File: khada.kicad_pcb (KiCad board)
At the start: 2 copper layers, 154.2 x 111.4 mm, 56 parts, among them J1 MJ-4PP-9, SW1 SW_Push, SW10 SW_Push, SW11 SW_Push, SW12 SW_Push, SW13 SW_Push, SW14 SW_Push, SW15 SW_Push, SW16 SW_Push, SW17 SW_Push, SW18 SW_Push, SW19 SW_Push, SW2 SW_Push, SW20 SW_Push, SW21 SW_Push, SW22 SW_Push, SW3 SW_Push, SW4 SW_Push, SW5 SW_Push, SW6 SW_Push, SW7 SW_Push, SW8 SW_Push, SW9 SW_Push, U1 YAAJ_WeAct_BlackPill_Part_Lik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

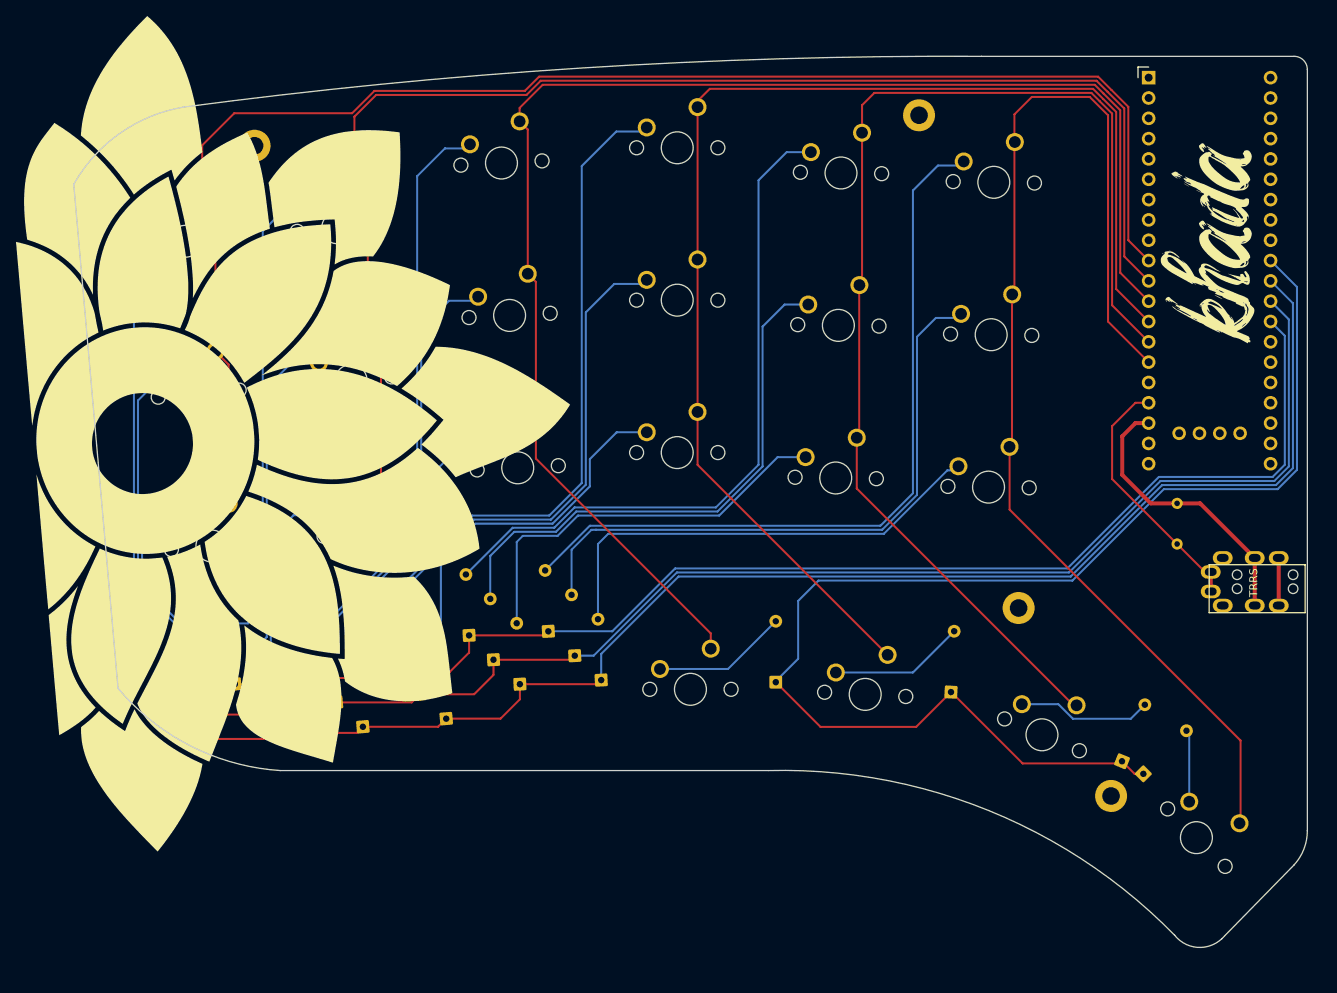
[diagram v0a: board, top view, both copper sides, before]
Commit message: cleaned up switch placement
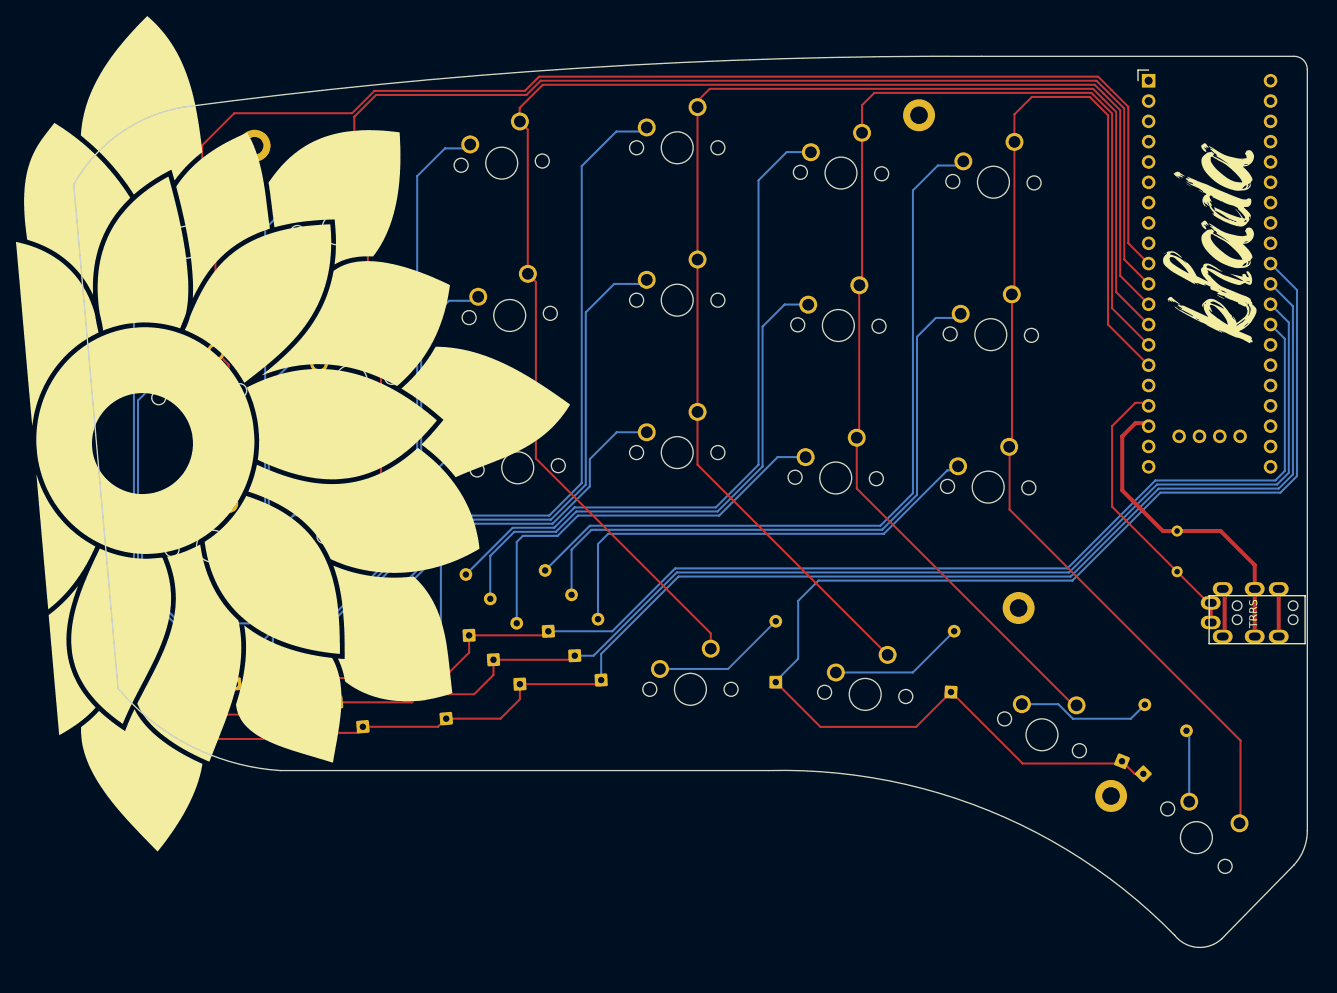
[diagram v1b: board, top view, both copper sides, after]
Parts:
- moved J1 3.87 mm to (204.7, 119.4)
- moved R1 3.45 mm to (188.7, 113.4)
- moved U1 0.38 mm to (185.2, 52.1)
- moved G*** 0.28 mm to (192.8, 72.4) (x2)
- moved SW4 0.15 mm to (83.8, 70.6)
- moved SW1 0.14 mm to (64.8, 72.3)
- moved SW2 0.10 mm to (66.5, 91.3)
- moved SW3 0.08 mm to (68.2, 110.2)
- moved SW5 0.06 mm to (85.5, 89.6)
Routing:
- net GND: track 0.00 -> 6.15 mm
- net +5V: track 35.6 -> 40.1 mm
- net DATA: track 32.0 -> 35.3 mm

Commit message: final design unless wiring incorrect
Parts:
- removed the G*** at (76.5, 94.9) (x2)
- added G***: LOGO, logo:designRed, F.Cu at (192.4, 85.2)
- added G***: LOGO, logo:lotusFront, F.Cu at (82.3, 85.1)
- added G***: LOGO, logo:lotusBack, B.Cu at (81.9, 85.3)
- added G***: LOGO, logo:designRed, B.Cu at (193.2, 85.2)
- SW1, SW10, SW12, SW13, SW14, SW15, SW16, SW17, SW18, SW19, SW2, SW20, SW21, SW22, SW3, SW4, SW5: footprint MX_Only:MXOnly-1U-NoLED -> switches:SW_MX_reversible_NoSilk
- SW11, SW6, SW7, SW8, SW9: footprint mx_only:MXOnly-1U-NoLED -> switches:SW_MX_reversible_NoSilk
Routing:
- net col5: track 147.8 -> 153.9 mm
- net col3: track 161.5 -> 166.7 mm
- net col4: track 150.7 -> 155.6 mm
- net Net-(D2-Pad2): track 38.5 -> 42.2 mm
- net col2: track 180.8 -> 184.5 mm
- net Net-(D19-Pad2): track 95.4 -> 98.7 mm
- net Net-(D20-Pad2): track 77.9 -> 81.1 mm
- net Net-(D21-Pad2): track 58.3 -> 61.5 mm
- net Net-(D6-Pad2): track 26.0 -> 29.1 mm
- net Net-(D5-Pad2): track 40.9 -> 44.0 mm
- net Net-(D4-Pad2): track 58.6 -> 61.7 mm
- net Net-(D22-Pad2): track 9.86 -> 12.9 mm
- net Net-(D13-Pad2): track 46.7 -> 49.8 mm
- net Net-(D16-Pad2): track 68.4 -> 71.4 mm
- net Net-(D17-Pad2): track 50.7 -> 53.7 mm
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- added copper zone on B.Cu, net GND
- added copper zone on F.Cu, net GND

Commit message: added encoder
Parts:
- added D23: D_Small, acheron_Components:D_THT_7.62mm_copy, F.Cu at (195.3, 125.9)
- added SW23: RotaryEncoder_Switch, keebio:RotaryEncoder_Alps_EC11E-Switch_Vertical_H20mm, F.Cu at (183.3, 115.1)
- moved R1 10.6 mm to (195.8, 105.5), turned to 0 degrees
- moved J1 6.54 mm to (204.9, 112.9)
- moved G*** 2.83 mm to (189.6, 85.2)
- moved G*** 2.83 mm to (190.0, 72.4) (x2)
- moved G*** 2.83 mm to (190.4, 85.2)
- moved U1 2.81 mm to (182.4, 51.8)
- renumbered D9 to D10, D14 to D11, D11 to D12, D12 to D13, D13 to D14, D18 to D15, D15 to D16, D16 to D17, D17 to D18, D22 to D19, D19 to D20, D20 to D21, D21 to D22, D10 to D7, D7 to D8, D8 to D9, SW9 to SW10, SW14 to SW11, SW11 to SW12, SW12 to SW13, SW13 to SW14, SW18 to SW15, SW15 to SW16, SW16 to SW17, SW17 to SW18, SW22 to SW19, SW19 to SW20, SW20 to SW21, SW21 to SW22, SW10 to SW7, SW7 to SW8, SW8 to SW9
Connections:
- J1 pad A: DATA -> unconnected-(J1-PadA)
- J1 pad B: unconnected-(J1-PadB) -> DATA
- R1 pad 1: DATA -> +5V
- R1 pad 2: +5V -> DATA
- SW11 pad 2: col3 -> col2
- SW15 pad 2: col4 -> col3
- SW19 pad 2: col5 -> col4
- SW7 pad 2: col2 -> col1
- U1 pad 10: col0 -> DATA
- U1 pad 16: unconnected-(U1-Pad16) -> ROTA
- U1 pad 17: DATA -> ROTB
- U1 pad 5: unconnected-(U1-Pad5) -> col0
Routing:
- net col5: track 153.9 -> 106.3 mm
- net col1: track 173.7 -> 220.0 mm
- net ROTA: track 0.00 -> 36.9 mm, vias 0 -> 1
- net ROTB: track 0.00 -> 34.3 mm, vias 0 -> 1
- net col4: track 155.6 -> 189.6 mm
- net Net-(D23-Pad2): track 0.00 -> 22.3 mm
- net row3: track 162.6 -> 183.6 mm
- net col3: track 166.7 -> 185.5 mm
- net col0: track 190.6 -> 174.4 mm
- net col2: track 184.5 -> 200.4 mm
- net DATA: track 37.1 -> 49.1 mm
- net +5V: track 39.9 -> 28.4 mm
- net unconnected-(J1-PadB): track 5.95 -> 0.00 mm
- net unconnected-(J1-PadA): track 0.00 -> 2.45 mm
- net row0: track 172.8 -> 174.5 mm
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
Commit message: edited switch footprint to have pads on both sides
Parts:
- SW1, SW10, SW11, SW12, SW13, SW14, SW15, SW16, SW17, SW18, SW19, SW2, SW20, SW21, SW22, SW3, SW4, SW5, SW6, SW7, SW8, SW9: footprint switches:SW_MX_reversible_NoSilk -> marbastlib-mx:SW_MX_Reversible_1u_PadsOnBothLayers
- moved D10 0.41 mm to (86.6, 128.6)
- moved D9 0.41 mm to (83.3, 125.6)
- moved D6 0.36 mm to (77.2, 129.4)
- moved D5 0.36 mm to (73.9, 126.4)
- moved D14 0.31 mm to (97.0, 127.7)
- moved D12 0.30 mm to (90.4, 121.9)
- moved D13 0.30 mm to (93.7, 124.7)
- moved D22 0.28 mm to (116.5, 122.9)
- moved D21 0.27 mm to (113.2, 119.9)
- moved D3 0.25 mm to (67.3, 130.3)
- moved D2 0.25 mm to (64.0, 127.3)
- moved D17 0.25 mm to (103.1, 120.4)
- moved D18 0.25 mm to (106.4, 123.4)
- moved D16 0.20 mm to (99.8, 117.6)
- moved D8 0.15 mm to (80.0, 122.8)
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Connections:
- U1 pad 10: DATA -> col0
- U1 pad 28: row0 -> DATA
- U1 pad 29: row1 -> row0
- U1 pad 30: row2 -> row1
- U1 pad 31: row3 -> row2
- U1 pad 32: unconnected-(U1-Pad32) -> row3
- U1 pad 5: col0 -> unconnected-(U1-Pad5)
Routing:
- net GND: track 5.44 -> 101.8 mm, vias 0 -> 2
- net DATA: track 49.1 -> 36.8 mm
- net col0: track 174.4 -> 186.1 mm
- net col1: track 220.0 -> 218.1 mm
- net col4: track 189.6 -> 187.9 mm
- net col2: track 200.4 -> 198.8 mm
- net row3: track 183.6 -> 184.3 mm
- net row0: track 174.5 -> 173.8 mm
- net row2: track 178.7 -> 178.0 mm
- net row1: track 175.4 -> 174.9 mm
- net ROTB: vias 1 -> 0
- net ROTA: vias 1 -> 0
- removed copper zone on B.Cu, net GND
- removed copper zone on F.Cu, net GND
